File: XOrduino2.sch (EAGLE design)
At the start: 81 parts, among them J1 2.5mm, J2 2.5mm, J3 2.5mm, J4 2.5mm, J5 Batt In, J6 MOT R, J7 MOT L, P1 10k, Q1 ALS-PT204-6C/L177, SW1 RESET, SW2 6mm Button, SW3 LEFT BUMPER, SW4 RIGHT BUMPER, U1 ATMEGA32U4-XUAU, U2 LMV358, U3 NJU7261, U4 DRV8833PWP, U5 QRE1113GR, U6 QRE1113GR, X1 USBPCB, X2 USBMINIB, X3 USBMICROB, Y1 16MHz

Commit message: 97% routed 4-layer XOrduino.
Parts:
- added JP12: SERVO, SparkFun-Connectors:M03PTH
- JP1, JP7, JP8, JP9: device xorduino:SOLDERJUMPERBOT-NOCONFLICT -> xorduino:SOLDERJUMPERBOT-VIA-NOCONFLICT
- X3: value USBMICROB -> USBMICROB-VIA; device xorduino:USBMICROB -> xorduino:USBMICROB-VIA
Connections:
- removed net N$17: D4.A, J5.1
- new net VCCIO: C14.1, C15.2, D3.C, D4.C, JP12.2, L3.1, LED5.A, RN5C.1, RN5D.1, RN6A.1, RN6B.1, U3.VIN, U4.VM
- net A4: now also JP7.2; no longer JP7.1
- net A5: now also JP8.2; no longer JP8.1
- net D2/SDA: now also JP1.2; no longer JP1.1
- net D4: now also JP9.2; no longer JP9.1
- net D7: now also JP10.2
- net GND: now also JP12.1
- net IO8: now also JP11.2; no longer JP10.2
- net IO9*: now also JP12.3; no longer JP11.2
- net LIGHT: now also JP8.1; no longer JP8.2
- net N$12: now also JP1.1; no longer JP1.2
- net SLIDER: now also JP9.1; no longer JP9.2
- net SOUND: now also JP7.1; no longer JP7.2
- net VIN: now also D4.A, J5.1; no longer C14.1, C15.2, D3.C, D4.C, L3.1, LED5.A, RN5C.1, RN5D.1, RN6A.1, RN6B.1, U3.VIN, U4.VM
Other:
- moved on the sheet: JP1, JP7, JP8, JP9

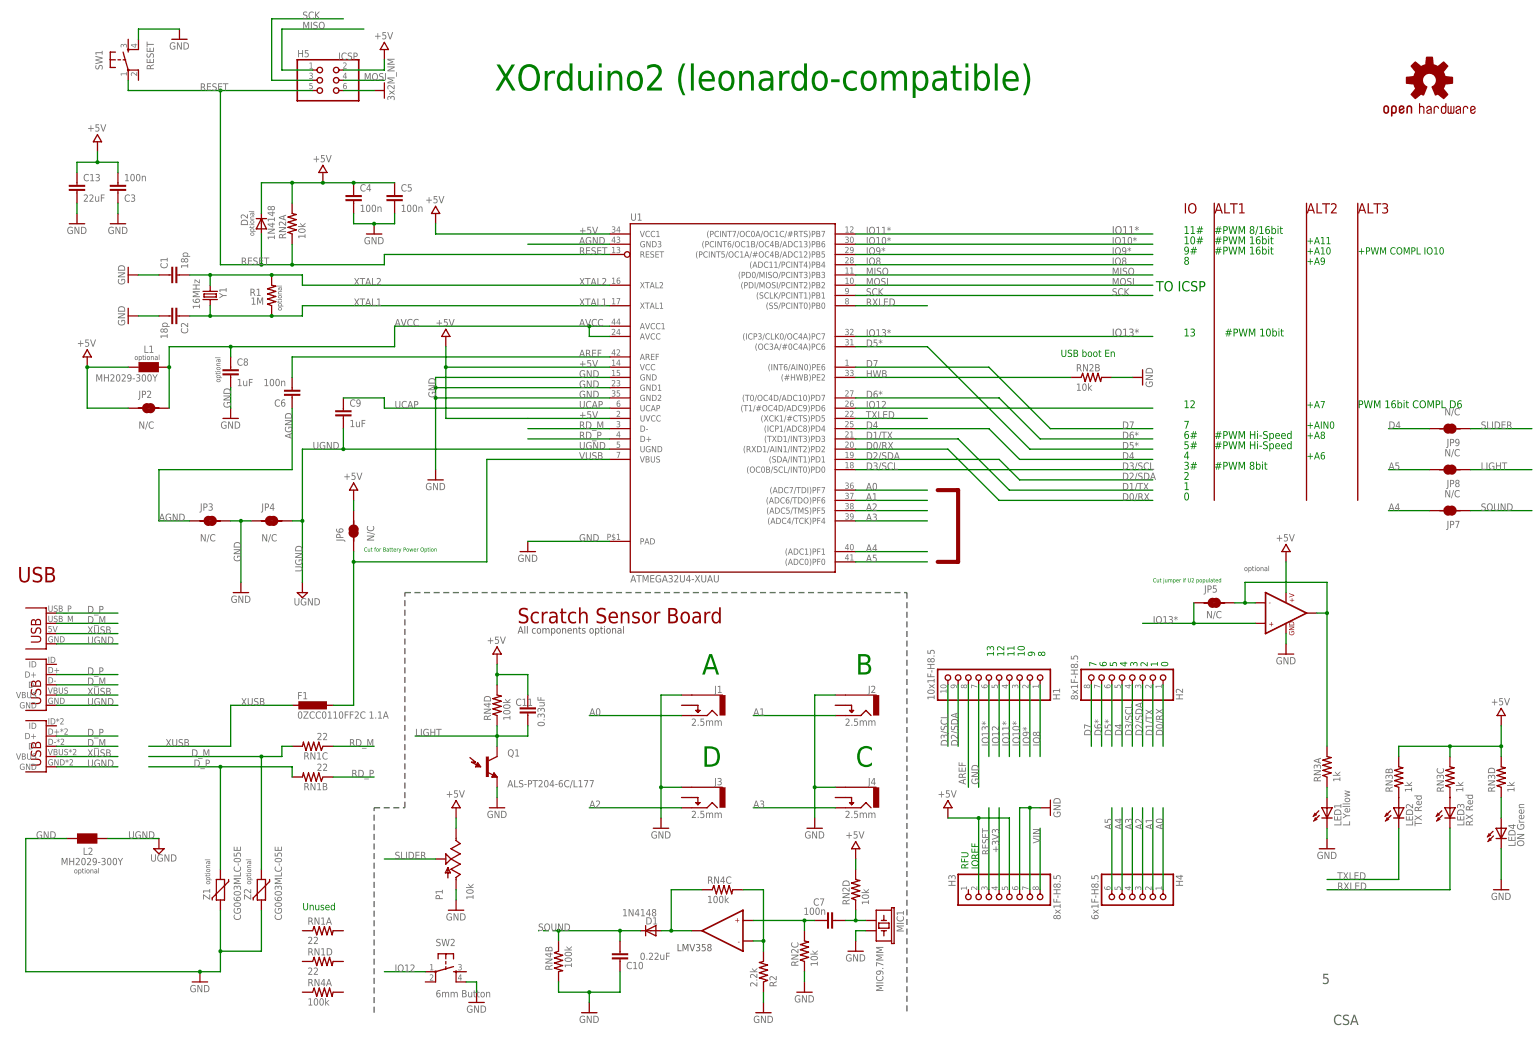
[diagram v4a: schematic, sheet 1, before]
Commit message: Tweaks for better 2-layer routability.
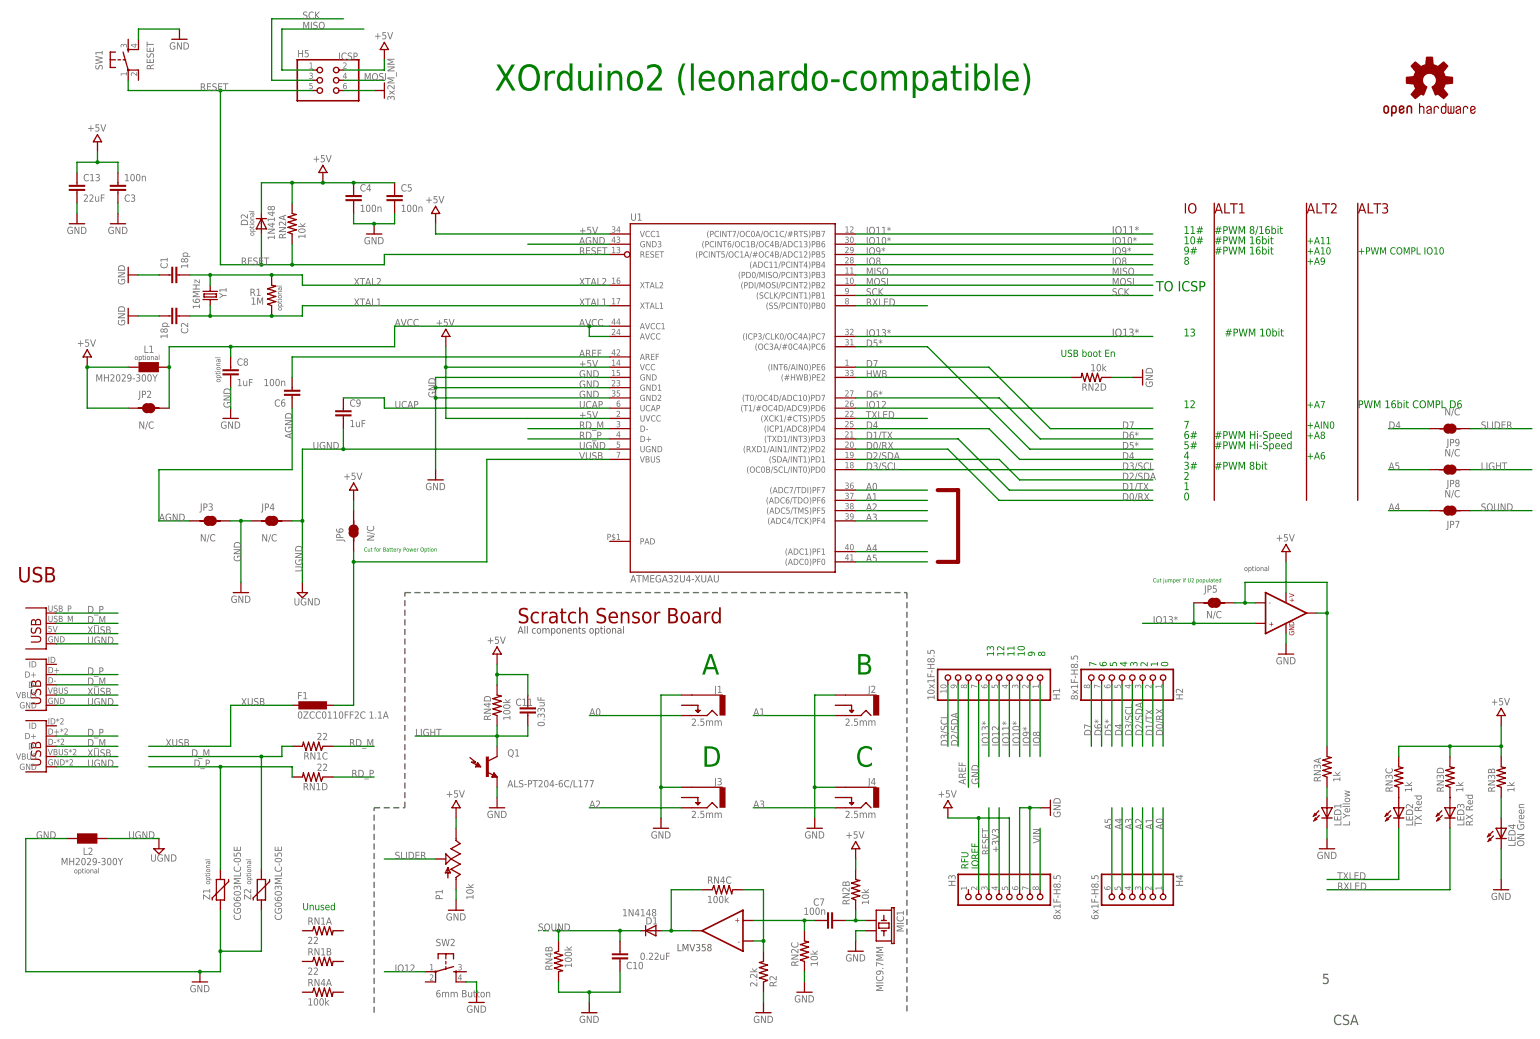
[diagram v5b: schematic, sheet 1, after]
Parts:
- JP1: device xorduino:SOLDERJUMPERBOT-VIA-NOCONFLICT -> xorduino:SOLDERJUMPERNOCONFLICT
- JP10, JP11: device xorduino:SOLDERJUMPERBOT-NOCONFLICT -> xorduino:SOLDERJUMPERBOT-VIA-NOCONFLICT
- LED1, LED2, LED3, LED4, LED5: device led:LED3MM -> xorduino:LED0805
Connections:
- net +5V: now also RN2B.2, RN5C.1, RN5D.1; no longer RN2D.2, RN5A.1, RN5B.1
- net D7: now also JP10.1; no longer JP10.2
- net D_P: now also RN1D.2; no longer RN1B.2
- net GND: now also RN2D.1; no longer RN2B.2, U1.PAD
- net HWB: now also RN2D.2; no longer RN2B.1
- net N$1: now also RN3D.1; no longer RN3C.1
- net N$19: now also RN7A.1, RN7B.1; no longer RN7C.1, RN7D.1
- net N$20: now also RN7C.1, RN7D.1; no longer RN7A.1, RN7B.1
- net N$21: now also JP10.2, RN5C.2; no longer JP10.1, RN5A.2
- net N$22: now also RN5D.2; no longer RN5B.2
- net N$3: now also RN3B.1; no longer RN3D.1
- net N$4: now also RN3C.1; no longer RN3B.1
- net N$8: now also RN5A.2, RN5B.2; no longer RN5C.2, RN5D.2
- net N$9: now also RN2B.1; no longer RN2D.1
- net RD_P: now also RN1D.1; no longer RN1B.1
- net VCCIO: now also RN5A.1, RN5B.1; no longer RN5C.1, RN5D.1
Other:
- moved on the sheet: JP10, RN1B, RN1D, RN2B, RN2D, RN3B, RN3C, RN3D, RN5A, RN5B, RN5C, RN5D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

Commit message: v5 gerbers.
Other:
- note added: "XXX: C4 optional, not near power pins"
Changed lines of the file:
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@@
 <text x="73.66" y="-5.08" size="5.08" layer="91">C</text>
 <text x="35.56" y="-5.08" size="5.08" layer="91">D</text>
+<text x="-50.8" y="142.24" size="1.778" layer="91">XXX: C4 optional, not near power pins</text>
 </plain>
 <instances>

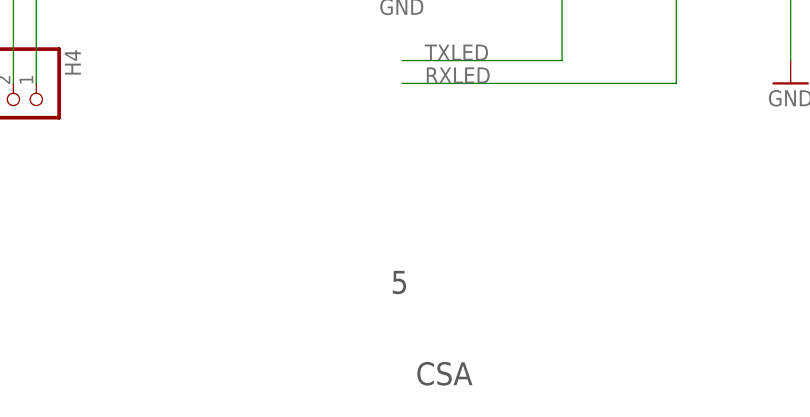
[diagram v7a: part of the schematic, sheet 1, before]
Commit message: Xorduino v6: rerouting with bigger vias, 10 mil traces, and better spacing.
Also added silkscreen, etc. and regenerated PDFs.
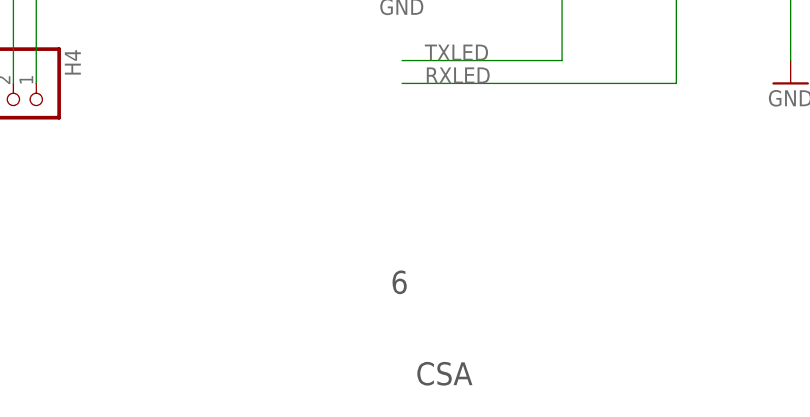
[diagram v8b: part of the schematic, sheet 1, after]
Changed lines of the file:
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@@
 <text x="-120.142" y="-31.496" size="1.27" layer="97">optional</text>
 <text x="169.926" y="43.434" size="1.27" layer="97">optional</text>
-<text x="189.23" y="-58.928" size="2.54" layer="97">5</text>
+<text x="189.23" y="-58.928" size="2.54" layer="97">6</text>
 <text x="192.024" y="-69.088" size="2.54" layer="97">CSA</text>
 <text x="40.64" y="30.48" size="3.81" layer="94" ratio="10" rot="MR0">Scratch Sensor Board</text>
@@
 <text x="167.64" y="63.5" size="1.778" layer="91">Unused</text>
 <text x="38.1" y="27.94" size="1.016" layer="91">Must be 20k-75k</text>
+<text x="172.72" y="7.62" size="5.08" layer="91">CSA</text>
 </plain>
 <instances>
